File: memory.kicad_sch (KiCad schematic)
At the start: 29 parts, among them U10 TPS2117DRLR, U2 SDINBDG4-8G, U9 TPS2117DRLR

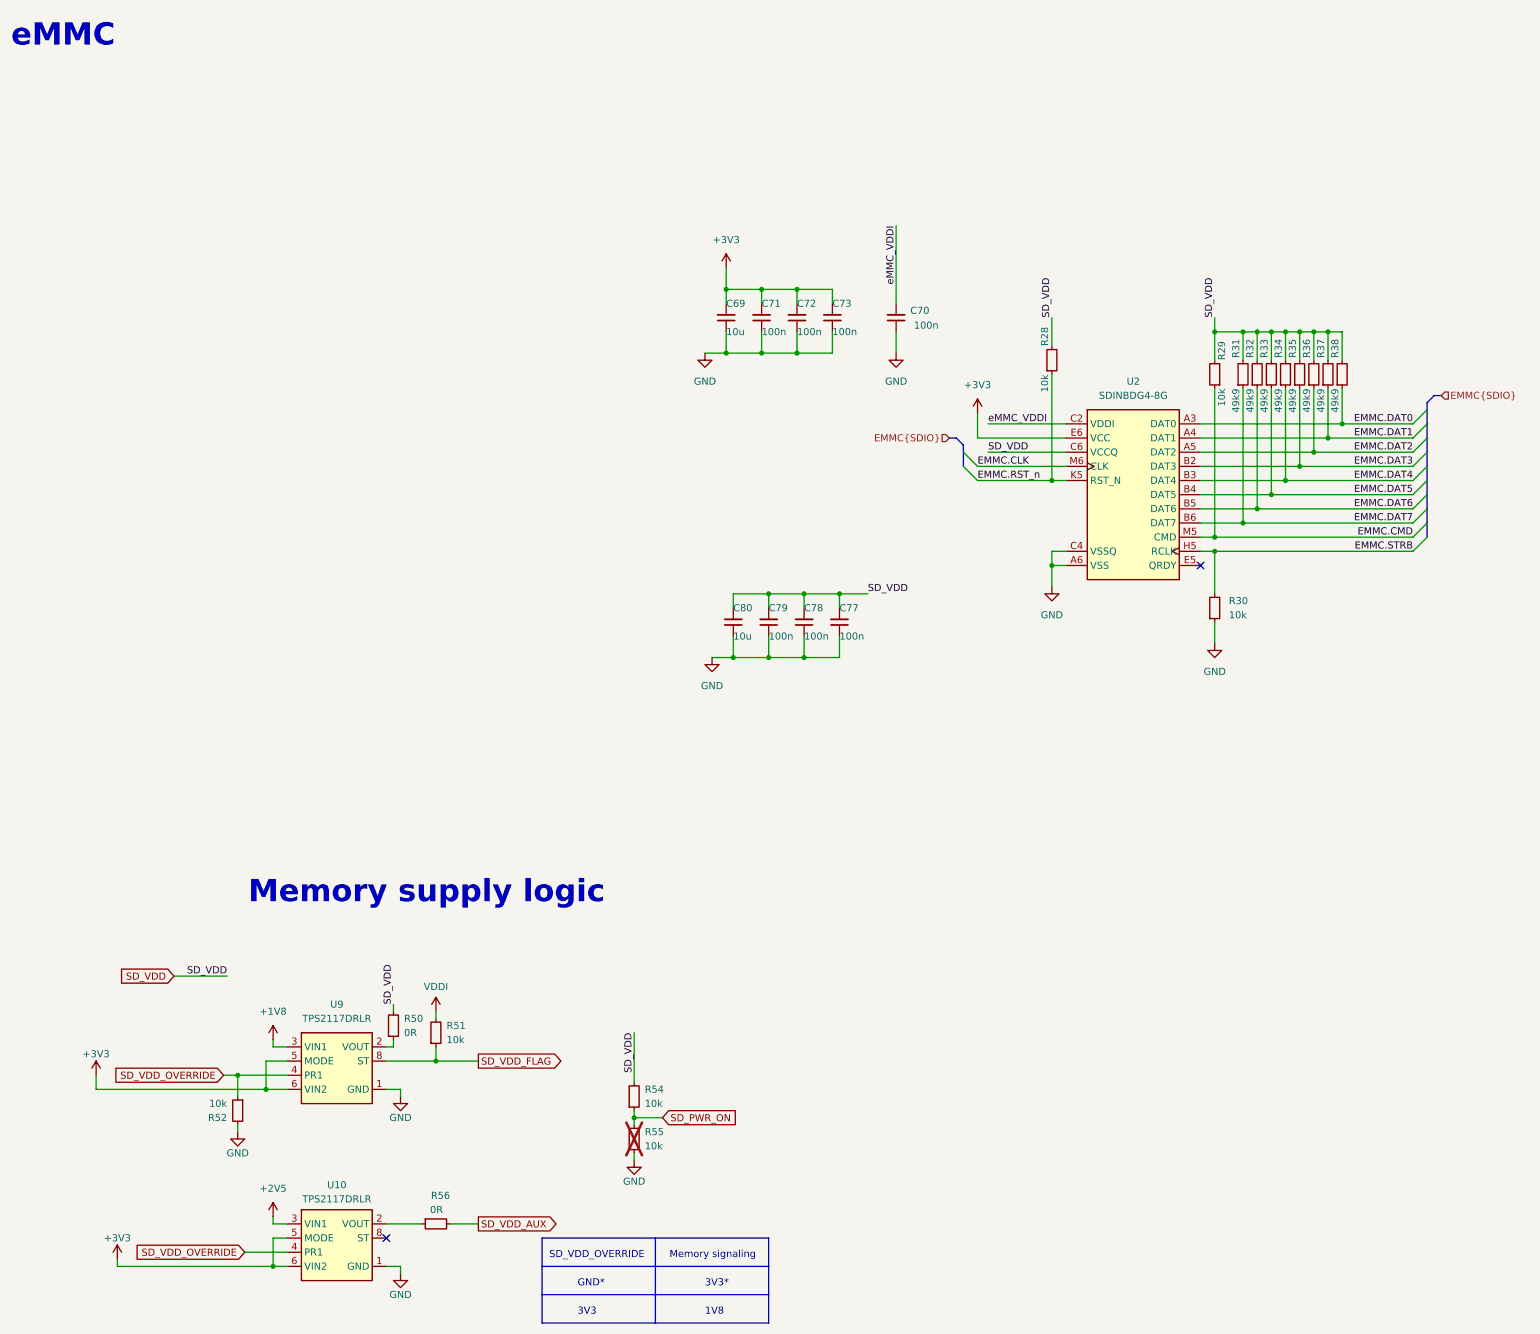
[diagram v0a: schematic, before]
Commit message: [#59910] Align buses, updated symbols and clean ERC
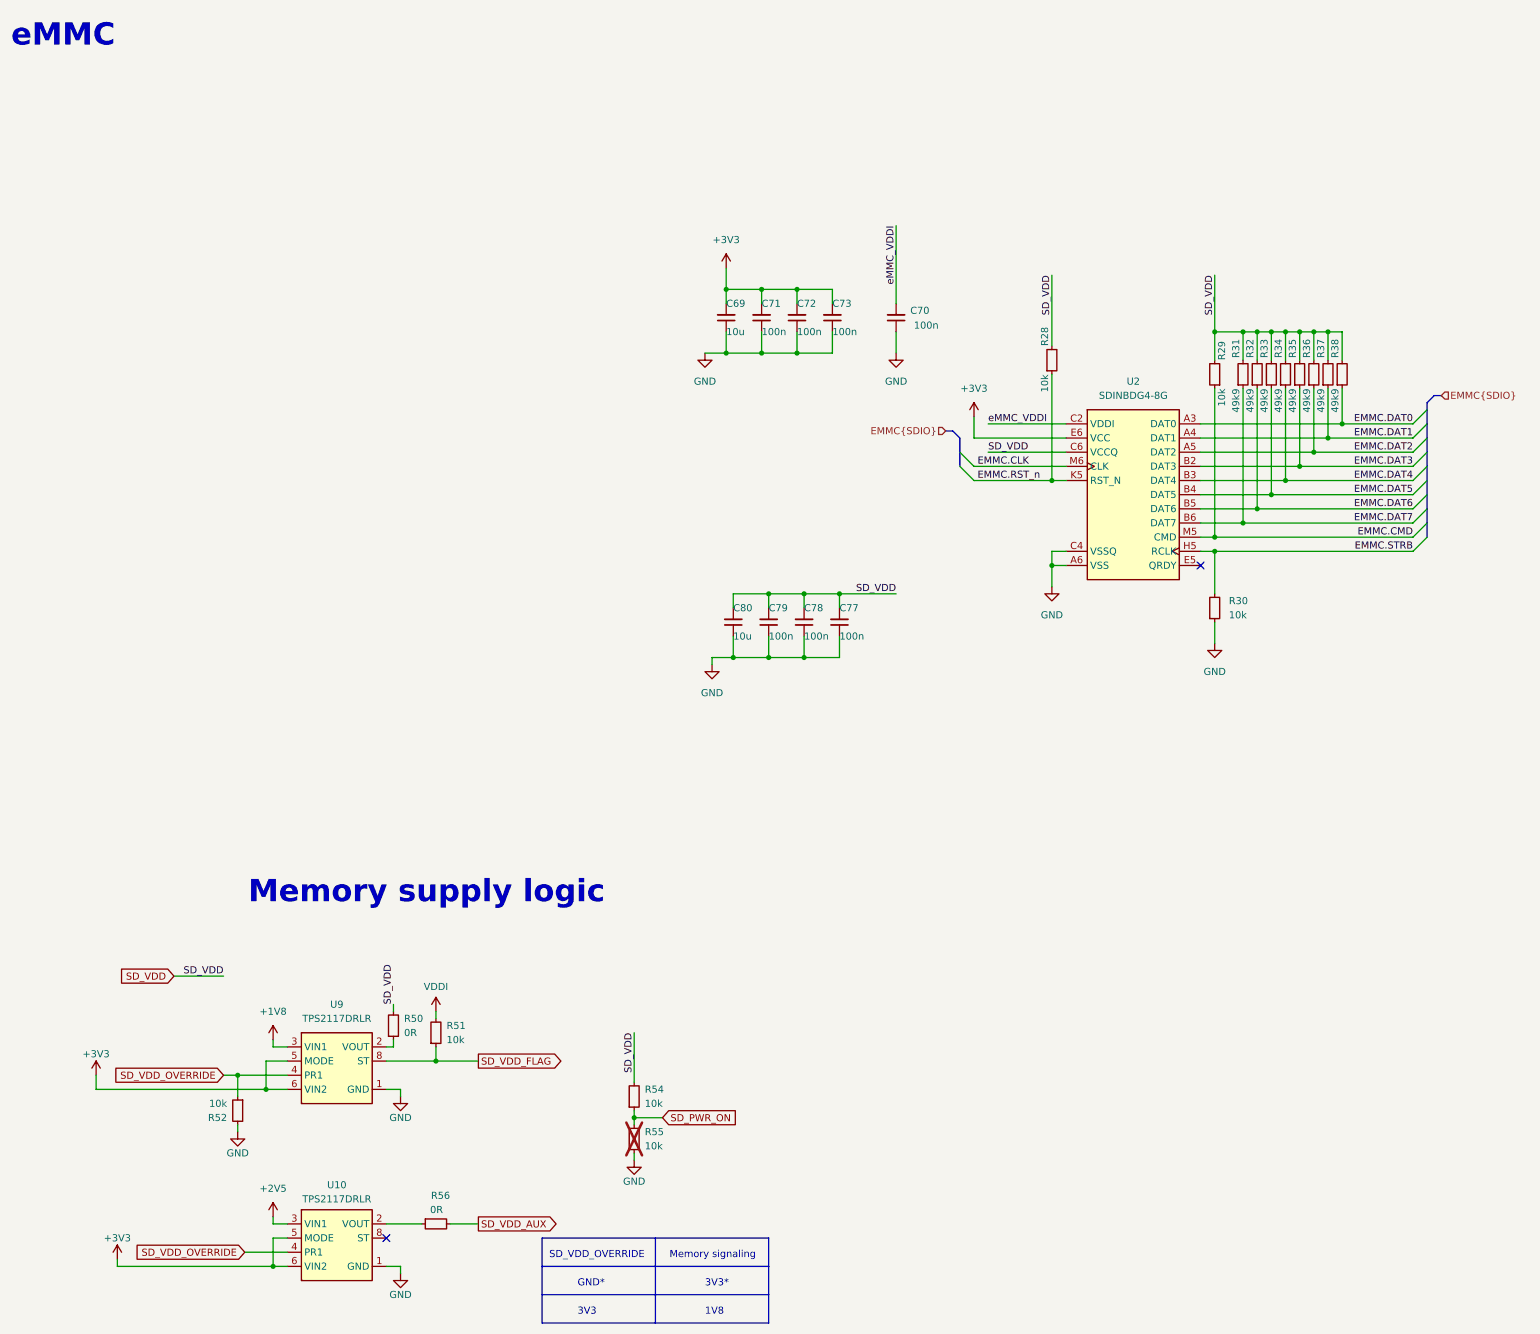
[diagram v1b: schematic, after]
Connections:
- net VDDI renamed VDD

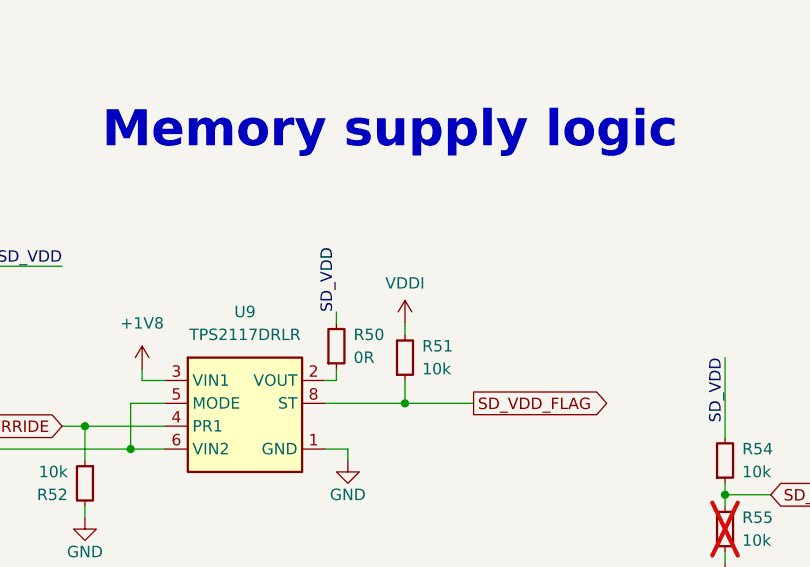
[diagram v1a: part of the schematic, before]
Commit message: [#73079] Migrate project to KiCad 8. Clean DRCs
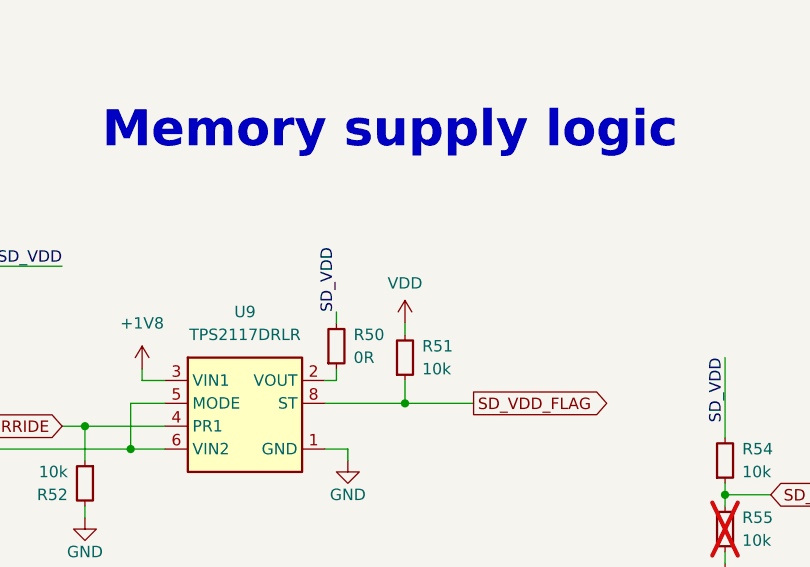
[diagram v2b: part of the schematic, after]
